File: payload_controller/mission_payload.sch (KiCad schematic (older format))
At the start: 21 parts, among them J3 Conn_01x08_Female, J4 Conn_02x07_Odd_Even, J6 Conn_01x03_Male, U33 ICL7660CSAT, U34 MSP430FR5969IRGZR, Y1 CM8V-T1A

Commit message: Continuing layout
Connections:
- net FAULT: now also J3.6 (Pin_6); no longer J3.5 (Pin_5)
- net PAYLOAD_RST: now also J3.5 (Pin_5); no longer J3.6 (Pin_6)
- net ALERT: now reaches U34.33 (P4.4/TB0.5)
- net BUSY_IN: no longer names the net of U34.19 (P4.3/A11)
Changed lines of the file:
@@
 Text HLabel 4300 3450 0    50   Input ~ 0
 ADC_SYNC
-Text HLabel 7350 3350 2    50   Output ~ 0
-BUSY_IN
 Text HLabel 4300 3350 0    50   Input ~ 0
 REVERSE_BIAS
@@
 Text GLabel 4300 3550 0    50   Input ~ 0
 TX_OUT
+Text GLabel 1800 4300 2    50   Input ~ 0
+FAULT
+Wire Wire Line
+	2650 2050 3000 2050
 Text GLabel 1800 4400 2    50   Input ~ 0
-FAULT
-Wire Wire Line
-	2650 2050 3000 2050
-Text GLabel 1800 4300 2    50   Input ~ 0
 PAYLOAD_RST
 Text GLabel 7350 2950 2    50   Input ~ 0
@@
 	0    1    1    0
 $EndComp
+Text HLabel 7350 3450 2    50   Output ~ 0
+ALERT
 $EndSCHEMATC

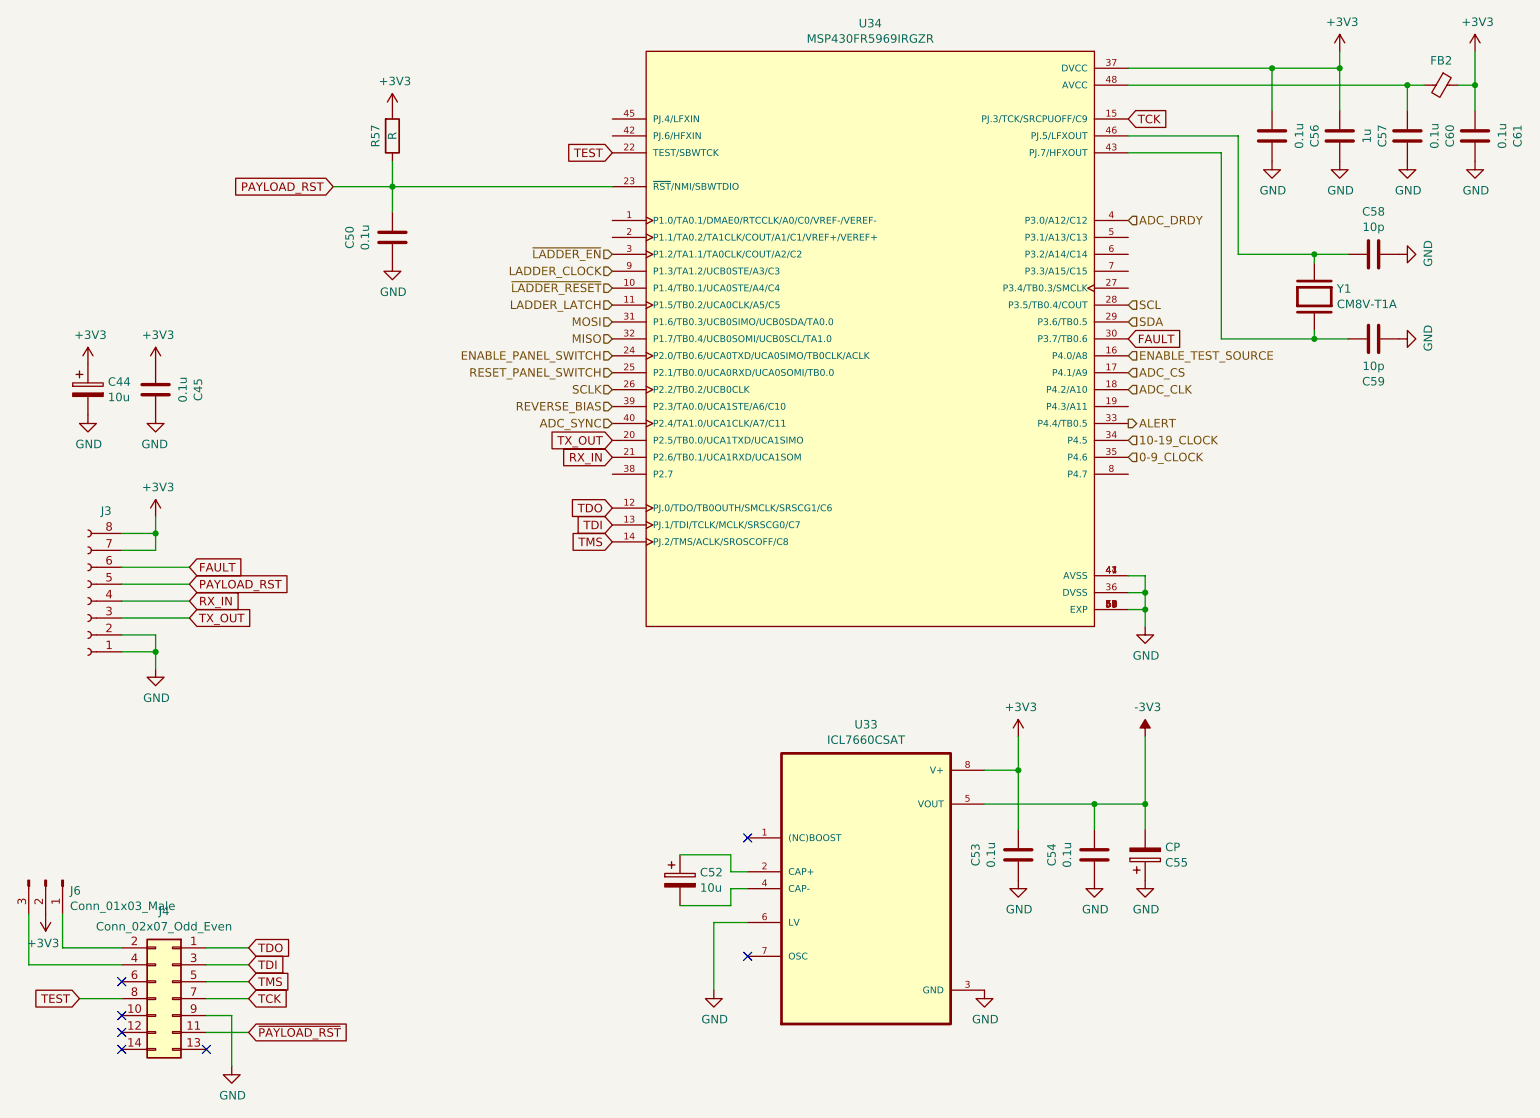
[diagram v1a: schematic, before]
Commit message: Continuing payload design
- Add OR gate for reverse bias
- Add GaAs panel connectors
- Add 3D models
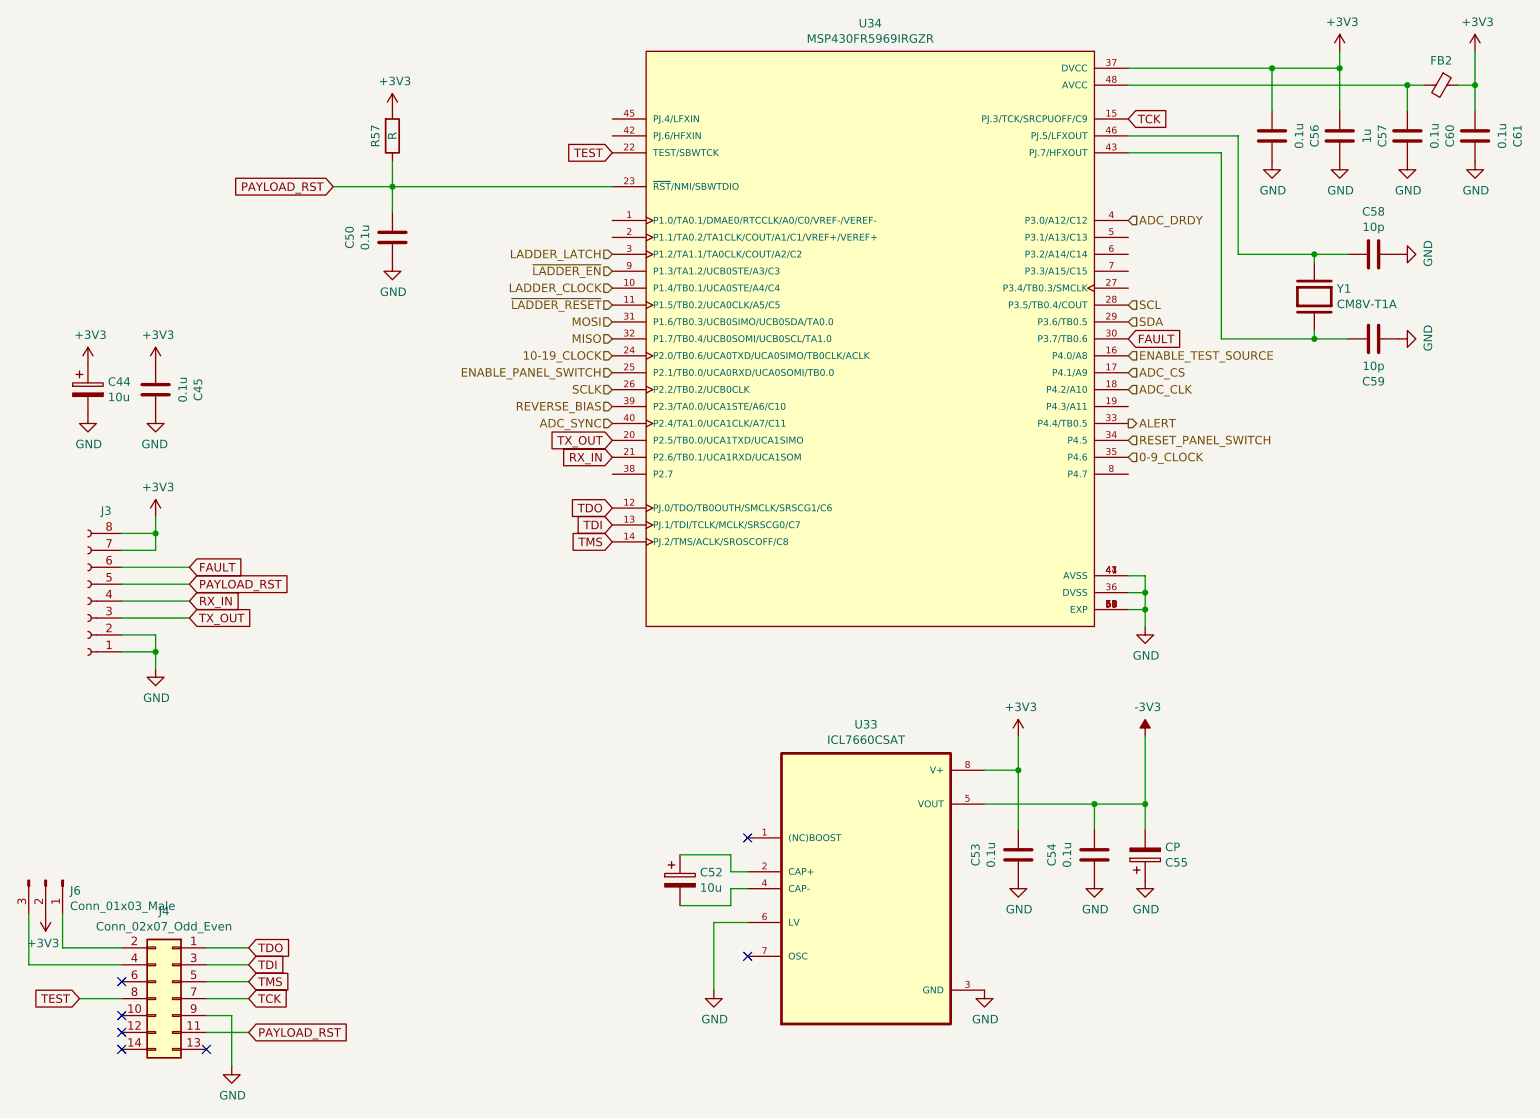
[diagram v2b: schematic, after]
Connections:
- net ~PAYLOAD_RST is gone; now on net PAYLOAD_RST: J4.11 (Pin_11)
- net 10-19_CLOCK: now also U34.24 (P2.0/TB0.6/UCA0TXD/UCA0SIMO/TB0CLK/ACLK); no longer U34.34 (P4.5)
- net ENABLE_PANEL_SWITCH: now also U34.25 (P2.1/TB0.0/UCA0RXD/UCA0SOMI/TB0.0); no longer U34.24 (P2.0/TB0.6/UCA0TXD/UCA0SIMO/TB0CLK/ACLK)
- net LADDER_CLOCK: now also U34.10 (P1.4/TB0.1/UCA0STE/A4/C4); no longer U34.9 (P1.3/TA1.2/UCB0STE/A3/C3)
- net LADDER_LATCH: now also U34.3 (P1.2/TA1.1/TA0CLK/COUT/A2/C2); no longer U34.11 (P1.5/TB0.2/UCA0CLK/A5/C5)
- net RESET_PANEL_SWITCH: now also U34.34 (P4.5); no longer U34.25 (P2.1/TB0.0/UCA0RXD/UCA0SOMI/TB0.0)
- net ~LADDER_EN: now also U34.9 (P1.3/TA1.2/UCB0STE/A3/C3); no longer U34.3 (P1.2/TA1.1/TA0CLK/COUT/A2/C2)
- net ~LADDER_RESET: now also U34.11 (P1.5/TB0.2/UCA0CLK/A5/C5); no longer U34.10 (P1.4/TB0.1/UCA0STE/A4/C4)
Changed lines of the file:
@@
 PAYLOAD_RST
 Text GLabel 2150 7050 2    50   Input ~ 0
-~PAYLOAD_RST
+PAYLOAD_RST
 Wire Wire Line
 	2150 7050 1900 7050
@@
 TEST
 Text HLabel 4300 3150 0    50   Input ~ 0
-RESET_PANEL_SWITCH
-Text HLabel 4300 3050 0    50   Input ~ 0
 ENABLE_PANEL_SWITCH
-Text HLabel 7350 3550 2    50   Input ~ 0
-10-19_CLOCK
 Text HLabel 7350 3650 2    50   Input ~ 0
 0-9_CLOCK
@@
 Text HLabel 7350 2850 2    50   Input ~ 0
 SDA
+Text HLabel 4300 2550 0    50   Input ~ 0
+~LADDER_EN
+Text HLabel 4300 2650 0    50   Input ~ 0
+LADDER_CLOCK
+Text HLabel 4300 2750 0    50   Input ~ 0
+~LADDER_RESET
 Text HLabel 4300 2450 0    50   Input ~ 0
-~LADDER_EN
-Text HLabel 4300 2550 0    50   Input ~ 0
-LADDER_CLOCK
-Text HLabel 4300 2650 0    50   Input ~ 0
-~LADDER_RESET
-Text HLabel 4300 2750 0    50   Input ~ 0
 LADDER_LATCH
 $Comp
@@
 Text HLabel 7350 3450 2    50   Output ~ 0
 ALERT
+Text HLabel 7350 3550 2    50   Input ~ 0
+RESET_PANEL_SWITCH
+Text HLabel 4300 3050 0    50   Input ~ 0
+10-19_CLOCK
 $EndSCHEMATC

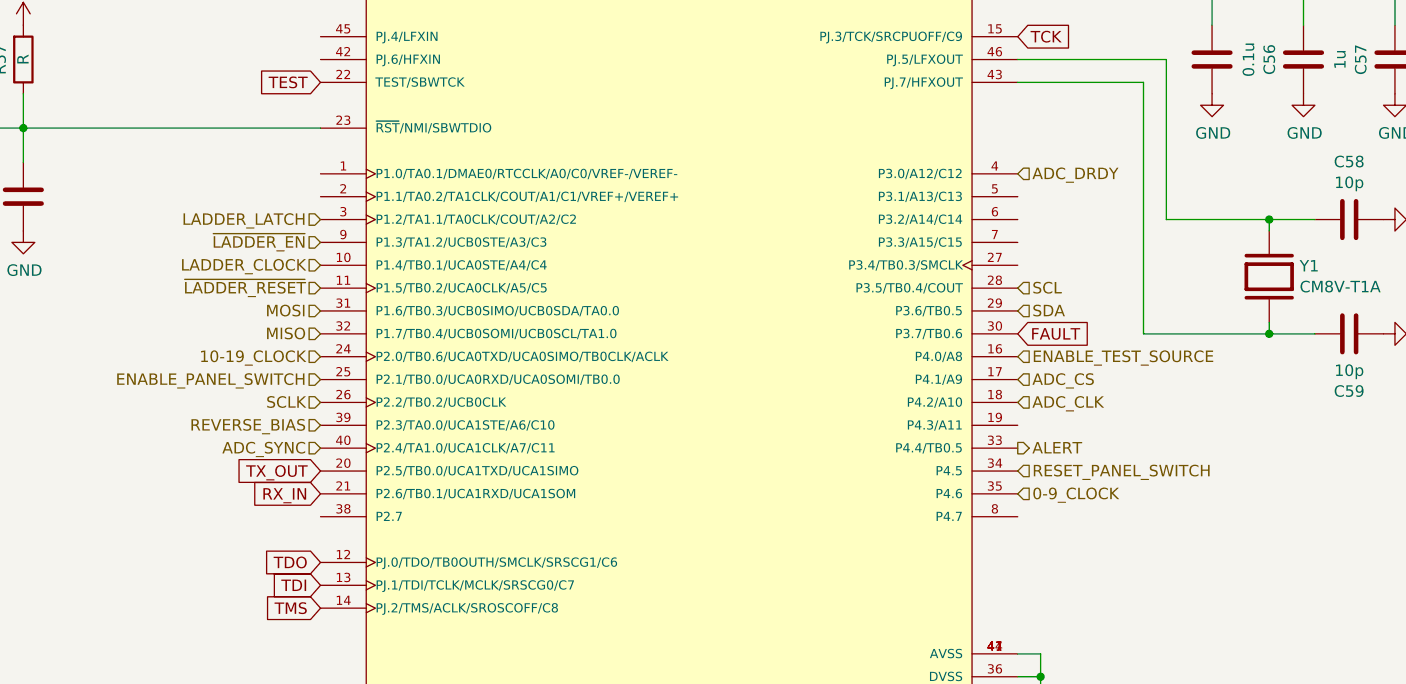
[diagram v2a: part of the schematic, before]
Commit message: Completed routing
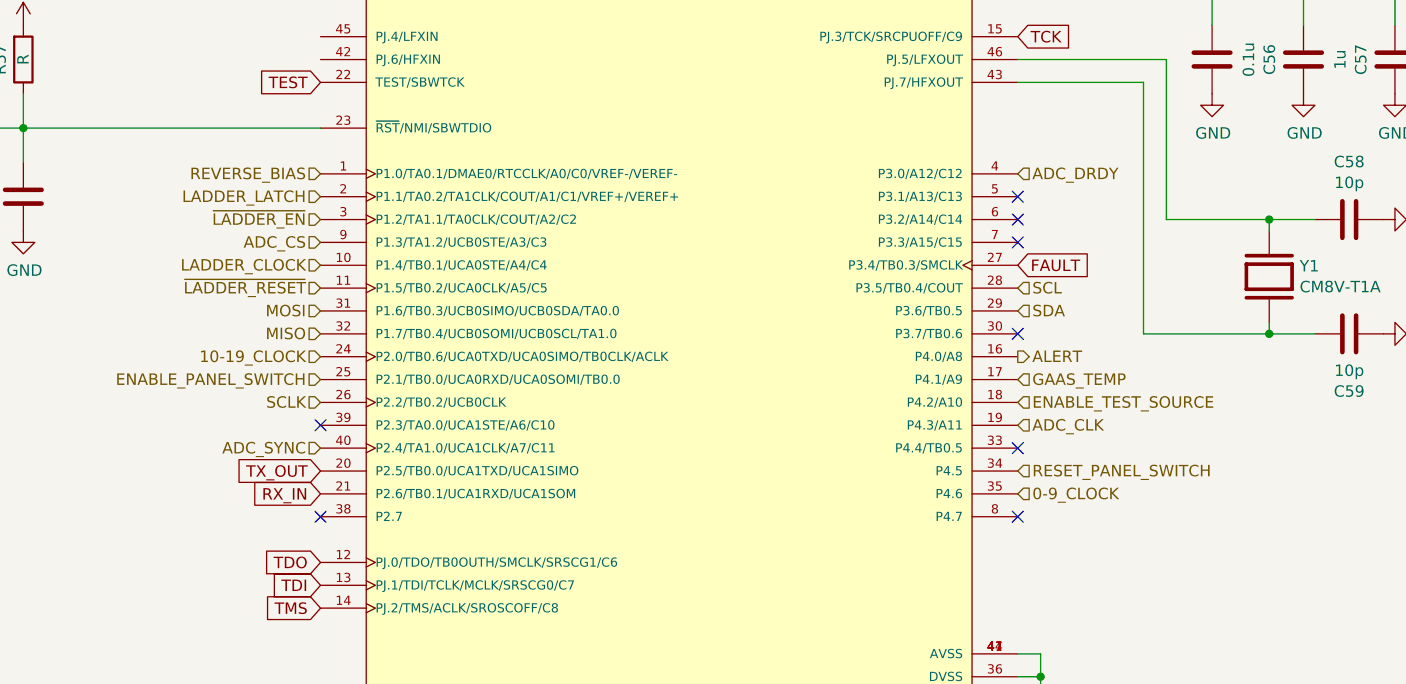
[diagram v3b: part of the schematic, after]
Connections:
- net ADC_CLK: now also U34.19 (P4.3/A11); no longer U34.18 (P4.2/A10)
- net ADC_CS: now also U34.9 (P1.3/TA1.2/UCB0STE/A3/C3); no longer U34.17 (P4.1/A9)
- net ALERT: now also U34.16 (P4.0/A8); no longer U34.33 (P4.4/TB0.5)
- net ENABLE_TEST_SOURCE: now also U34.18 (P4.2/A10); no longer U34.16 (P4.0/A8)
- net FAULT: now also U34.27 (P3.4/TB0.3/SMCLK); no longer U34.30 (P3.7/TB0.6)
- net LADDER_LATCH: now also U34.2 (P1.1/TA0.2/TA1CLK/COUT/A1/C1/VREF+/VEREF+); no longer U34.3 (P1.2/TA1.1/TA0CLK/COUT/A2/C2)
- net REVERSE_BIAS: now also U34.1 (P1.0/TA0.1/DMAE0/RTCCLK/A0/C0/VREF-/VEREF-); no longer U34.39 (P2.3/TA0.0/UCA1STE/A6/C10)
- net ~LADDER_EN: now also U34.3 (P1.2/TA1.1/TA0CLK/COUT/A2/C2); no longer U34.9 (P1.3/TA1.2/UCB0STE/A3/C3)
- new net GAAS_TEMP: U34.17 (P4.1/A9)
- no-connect marks 7 -> 15
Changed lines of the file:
@@
 Text HLabel 7350 3650 2    50   Input ~ 0
 0-9_CLOCK
-Text HLabel 7350 3050 2    50   Input ~ 0
+Text HLabel 7350 3250 2    50   Input ~ 0
 ENABLE_TEST_SOURCE
 Text HLabel 7350 2750 2    50   Input ~ 0
@@
 Text HLabel 7350 2850 2    50   Input ~ 0
 SDA
-Text HLabel 4300 2550 0    50   Input ~ 0
+Text HLabel 4300 2450 0    50   Input ~ 0
 ~LADDER_EN
 Text HLabel 4300 2650 0    50   Input ~ 0
@@
 Text HLabel 4300 2750 0    50   Input ~ 0
 ~LADDER_RESET
-Text HLabel 4300 2450 0    50   Input ~ 0
+Text HLabel 4300 2350 0    50   Input ~ 0
 LADDER_LATCH
 $Comp
@@
 Text HLabel 4300 2950 0    50   Input ~ 0
 MISO
-Text HLabel 7350 3250 2    50   Input ~ 0
+Text HLabel 7350 3350 2    50   Input ~ 0
 ADC_CLK
-Text HLabel 7350 3150 2    50   Input ~ 0
+Text HLabel 4300 2550 0    50   Input ~ 0
 ADC_CS
 Text HLabel 7350 2250 2    50   Input ~ 0
@@
 Text HLabel 4300 3450 0    50   Input ~ 0
 ADC_SYNC
-Text HLabel 4300 3350 0    50   Input ~ 0
+Text HLabel 4300 2250 0    50   Input ~ 0
 REVERSE_BIAS
 $Comp
@@
 Text GLabel 1800 4400 2    50   Input ~ 0
 PAYLOAD_RST
-Text GLabel 7350 2950 2    50   Input ~ 0
+Text GLabel 7350 2650 2    50   Input ~ 0
 FAULT
 Text GLabel 1800 4500 2    50   Input ~ 0
@@
 	0    1    1    0
 $EndComp
-Text HLabel 7350 3450 2    50   Output ~ 0
+Text HLabel 7350 3050 2    50   Output ~ 0
 ALERT
 Text HLabel 7350 3550 2    50   Input ~ 0
@@
 Text HLabel 4300 3050 0    50   Input ~ 0
 10-19_CLOCK
+NoConn ~ 4300 3350
+NoConn ~ 4300 3750
+NoConn ~ 7350 2350
+NoConn ~ 7350 2450
+NoConn ~ 7350 2550
+NoConn ~ 7350 2950
+NoConn ~ 7350 3450
+NoConn ~ 7350 3750
+Text HLabel 7350 3150 2    50   Input ~ 0
+GAAS_TEMP
 $EndSCHEMATC

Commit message: Generated manufacturing files
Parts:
- J4: value Conn_02x07_Odd_Even -> JTAG
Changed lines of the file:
@@
 Sheet 5 6
 Title ""
-Date ""
+Date "2022-11-30"
 Rev ""
 Comp "Advanced eXperimental Payloads | UNL Aerospace Club"
 Comment1 "Copyright (c) 2022"
 Comment2 "Designer: WSA"
-Comment3 "Reviewer:"
-Comment4 "Approved: "
+Comment3 "Reviewer: WSA"
+Comment4 "Approved: WSA"
 $EndDescr
 $Comp
@@
 AR Path="/63D21EEE/63D67CB6" Ref="J4"  Part="1"
 F 0 "J4" H 1750 7367 50  0000 C CNN
-F 1 "Conn_02x07_Odd_Even" H 1750 7276 50  0000 C CNN
+F 1 "JTAG" H 1750 7276 50  0000 C CNN
 F 2 "Connector_PinSocket_2.54mm:PinSocket_2x08_P2.54mm_Vertical" H 1700 6850 50  0001 C CNN
 F 3 "~" H 1700 6850 50  0001 C CNN
@@
 P 950 6150
 F 0 "J6" V 1012 6294 50  0000 L CNN
-F 1 "Conn_01x03_Male" V 1103 6294 50  0000 L CNN
+F 1 "Conn_01x03_Male" V 1103 6294 50  0001 L CNN
 F 2 "Connector_PinHeader_2.54mm:PinHeader_1x03_P2.54mm_Vertical" H 950 6150 50  0001 C CNN
 F 3 "~" H 950 6150 50  0001 C CNN
